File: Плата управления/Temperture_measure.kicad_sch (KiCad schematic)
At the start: 3 parts

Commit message: Версия под отчёт
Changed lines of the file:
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@@
   )
   (text "Температура транзисторов" (at 137.795 76.2 0)
-    (effects (font (size 2 2) bold) (justify left bottom))
+    (effects (font (size 2.5 2.5) bold) (justify left bottom))
   )
   (global_label "Temperature_Power_SDA_MCU" (shape bidirectional) (at 157.48 107.315 0) (fields_autoplaced)

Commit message: VER2.0
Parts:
- removed R17, R18, R19: 10k, Resistor_SMD:R_0603_1608Metric_Pad0.98x0.95mm_HandSolder, symbol Device:R_Small
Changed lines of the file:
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@@
     (comment 1 "МПСТ.76721.758764.02.Э3.М")
-  )
-  (junction (at 139.7 93.345) (diameter 0) (color 0 0 0 0)
-  )
-  (wire (pts (xy 157.48 107.315) (xy 130.81 107.315))
-    (stroke (width 0) (type default))
-  )
-  (wire (pts (xy 157.48 102.235) (xy 148.59 102.235))
-    (stroke (width 0) (type default))
-  )
-  (wire (pts (xy 139.7 93.345) (xy 139.7 94.615))
-    (stroke (width 0) (type default))
-  )
-  (wire (pts (xy 139.7 92.075) (xy 139.7 93.345))
-    (stroke (width 0) (type default))
-  )
-  (wire (pts (xy 139.7 104.775) (xy 139.7 99.695))
-    (stroke (width 0) (type default))
-  )
-  (wire (pts (xy 148.59 94.615) (xy 148.59 93.345))
-    (stroke (width 0) (type default))
-  )
-  (wire (pts (xy 148.59 102.235) (xy 148.59 99.695))
-    (stroke (width 0) (type default))
-  )
-  (wire (pts (xy 130.81 93.345) (xy 139.7 93.345))
-    (stroke (width 0) (type default))
-  )
-  (wire (pts (xy 139.7 93.345) (xy 148.59 93.345))
-    (stroke (width 0) (type default))
-  )
-  (wire (pts (xy 130.81 94.615) (xy 130.81 93.345))
-    (stroke (width 0) (type default))
-  )
-  (wire (pts (xy 130.81 107.315) (xy 130.81 99.695))
-    (stroke (width 0) (type default))
-  )
-  (wire (pts (xy 157.48 104.775) (xy 139.7 104.775))
-    (stroke (width 0) (type default))
   )
   (rectangle (start 125.095 76.835) (end 190.5 121.285)
@@
     (effects (font (size 2.5 2.5) bold) (justify left bottom))
   )
-  (global_label "Temperature_Power_SDA_MCU" (shape bidirectional) (at 157.48 107.315 0) (fields_autoplaced)
-    (effects (font (size 1.27 1.27)) (justify left))
-    (property "Intersheetrefs" "${INTERSHEET_REFS}" (at 189.3954 107.315 0)
-      (effects (font (size 1.27 1.27)) (justify left) hide)
-    )
-  )
-  (global_label "Temperature_Power_SCL_MCU" (shape input) (at 157.48 104.775 0) (fields_autoplaced)
-    (effects (font (size 1.27 1.27)) (justify left))
-    (property "Intersheetrefs" "${INTERSHEET_REFS}" (at 188.2236 104.775 0)
-      (effects (font (size 1.27 1.27)) (justify left) hide)
-    )
-  )
-  (global_label "Temperature_Power_~{OS}_MCU" (shape input) (at 157.48 102.235 0) (fields_autoplaced)
-    (effects (font (size 1.27 1.27)) (justify left))
-    (property "Intersheetrefs" "${INTERSHEET_REFS}" (at 187.256 102.235 0)
-      (effects (font (size 1.27 1.27)) (justify left) hide)
-    )
-  )
-  (symbol (lib_id "Device:R_Small") (at 148.59 97.155 180) (unit 1)
-    (in_bom yes) (on_board yes) (dnp no) (fields_autoplaced)
-    (property "Reference" "R19" (at 151.13 96.52 0)
-      (effects (font (size 1.27 1.27)) (justify right))
-    )
-    (property "Value" "10k" (at 151.13 99.06 0)
-      (effects (font (size 1.27 1.27)) (justify right))
-    )
-    (property "Footprint" "Resistor_SMD:R_0603_1608Metric_Pad0.98x0.95mm_HandSolder" (at 148.59 97.155 0)
-      (effects (font (size 1.27 1.27)) hide)
-    )
-    (property "Datasheet" "~" (at 148.59 97.155 0)
-      (effects (font (size 1.27 1.27)) hide)
-    )
-    (pin "1")
-    (pin "2")
-    (instances
-      (project "Плата управления"
-        (path "/75f4c67c-bbde-4446-8f82-67797a1b269f/d6b8b9ce-300b-4d22-9d4c-9182eba581b1"
-          (reference "R19") (unit 1)
-        )
-        (path "/75f4c67c-bbde-4446-8f82-67797a1b269f/c91ff3ec-ad20-4326-acd4-2c9dea437172"
-          (reference "R17") (unit 1)
-        )
-      )
-      (project "Силовая плата"
-        (path "/96c6fc92-8ec6-44f7-b0dc-9ad8f1acea09/1efb5faf-bb82-4ac6-a144-d6576b4720aa"
-          (reference "R2") (unit 1)
-        )
-      )
-    )
-  )
-  (symbol (lib_id "power:+3.3V") (at 139.7 92.075 0) (unit 1)
-    (in_bom yes) (on_board yes) (dnp no) (fields_autoplaced)
-    (property "Reference" "#PWR026" (at 139.7 95.885 0)
-      (effects (font (size 1.27 1.27)) hide)
-    )
-    (property "Value" "+3.3V" (at 139.7 88.265 0)
-      (effects (font (size 1.27 1.27)))
-    )
-    (property "Footprint" "" (at 139.7 92.075 0)
-      (effects (font (size 1.27 1.27)) hide)
-    )
-    (property "Datasheet" "" (at 139.7 92.075 0)
-      (effects (font (size 1.27 1.27)) hide)
-    )
-    (pin "1")
-    (instances
-      (project "Плата управления"
-        (path "/75f4c67c-bbde-4446-8f82-67797a1b269f/d6b8b9ce-300b-4d22-9d4c-9182eba581b1"
-          (reference "#PWR026") (unit 1)
-        )
-      )
-    )
-  )
-  (symbol (lib_id "Device:R_Small") (at 130.81 97.155 180) (unit 1)
-    (in_bom yes) (on_board yes) (dnp no) (fields_autoplaced)
-    (property "Reference" "R17" (at 133.35 96.52 0)
-      (effects (font (size 1.27 1.27)) (justify right))
-    )
-    (property "Value" "10k" (at 133.35 99.06 0)
-      (effects (font (size 1.27 1.27)) (justify right))
-    )
-    (property "Footprint" "Resistor_SMD:R_0603_1608Metric_Pad0.98x0.95mm_HandSolder" (at 130.81 97.155 0)
-      (effects (font (size 1.27 1.27)) hide)
-    )
-    (property "Datasheet" "~" (at 130.81 97.155 0)
-      (effects (font (size 1.27 1.27)) hide)
-    )
-    (pin "1")
-    (pin "2")
-    (instances
-      (project "Плата управления"
-        (path "/75f4c67c-bbde-4446-8f82-67797a1b269f/d6b8b9ce-300b-4d22-9d4c-9182eba581b1"
-          (reference "R17") (unit 1)
-        )
-        (path "/75f4c67c-bbde-4446-8f82-67797a1b269f/c91ff3ec-ad20-4326-acd4-2c9dea437172"
-          (reference "R17") (unit 1)
-        )
-      )
-      (project "Силовая плата"
-        (path "/96c6fc92-8ec6-44f7-b0dc-9ad8f1acea09/1efb5faf-bb82-4ac6-a144-d6576b4720aa"
-          (reference "R2") (unit 1)
-        )
-      )
-    )
-  )
-  (symbol (lib_id "Device:R_Small") (at 139.7 97.155 180) (unit 1)
-    (in_bom yes) (on_board yes) (dnp no) (fields_autoplaced)
-    (property "Reference" "R18" (at 142.24 96.52 0)
-      (effects (font (size 1.27 1.27)) (justify right))
-    )
-    (property "Value" "10k" (at 142.24 99.06 0)
-      (effects (font (size 1.27 1.27)) (justify right))
-    )
-    (property "Footprint" "Resistor_SMD:R_0603_1608Metric_Pad0.98x0.95mm_HandSolder" (at 139.7 97.155 0)
-      (effects (font (size 1.27 1.27)) hide)
-    )
-    (property "Datasheet" "~" (at 139.7 97.155 0)
-      (effects (font (size 1.27 1.27)) hide)
-    )
-    (pin "1")
-    (pin "2")
-    (instances
-      (project "Плата управления"
-        (path "/75f4c67c-bbde-4446-8f82-67797a1b269f/d6b8b9ce-300b-4d22-9d4c-9182eba581b1"
-          (reference "R18") (unit 1)
-        )
-        (path "/75f4c67c-bbde-4446-8f82-67797a1b269f/c91ff3ec-ad20-4326-acd4-2c9dea437172"
-          (reference "R17") (unit 1)
-        )
-      )
-      (project "Силовая плата"
-        (path "/96c6fc92-8ec6-44f7-b0dc-9ad8f1acea09/1efb5faf-bb82-4ac6-a144-d6576b4720aa"
-          (reference "R2") (unit 1)
-        )
-      )
-    )
-  )
 )

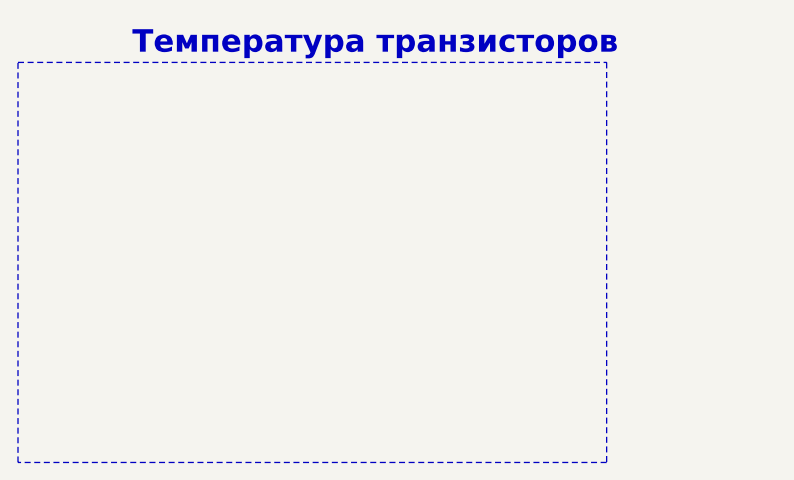
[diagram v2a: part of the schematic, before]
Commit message: Добавил NTC обработку
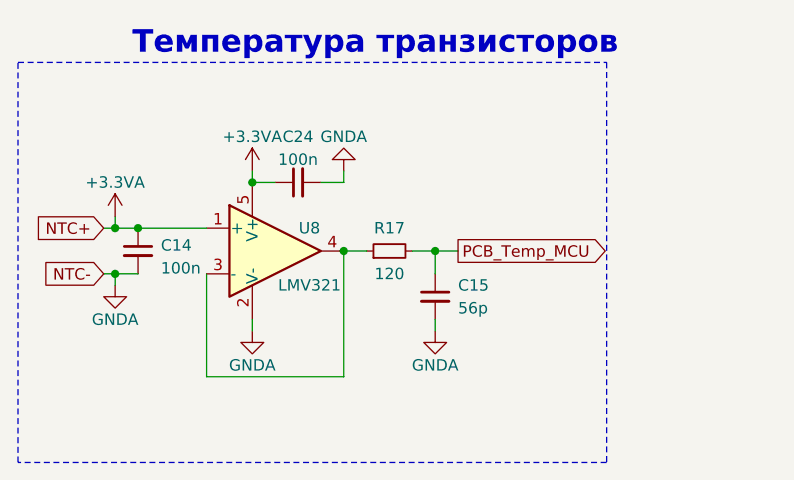
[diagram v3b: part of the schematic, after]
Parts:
- added C14, C24: 100n, Capacitor_SMD:C_0603_1608Metric_Pad1.08x0.95mm_HandSolder, symbol Device:C_Small
- added C15: 56p, Capacitor_SMD:C_0603_1608Metric_Pad1.08x0.95mm_HandSolder, symbol Device:C_Small
- added R17: 120, Resistor_SMD:R_0603_1608Metric_Pad0.98x0.95mm_HandSolder, symbol Device:R_Small
- added U8: LMV321, Package_TO_SOT_SMD:SOT-23-5_HandSoldering, symbol Amplifier_Operational:LMV321
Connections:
- new net: R17.1, U8.3 (-), U8.4
- new net +3.3VA: C14.1, C24.1, U8.1 (+), U8.5 (V+)
- new net GNDA: C14.2, C15.2, C24.2, U8.2 (V-)
- new net PCB_Temp_MCU: C15.1, R17.2

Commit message: Новые драйвера и разъёмы
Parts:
- added C42, C43, C47, C50: 100n, Capacitor_SMD:C_0603_1608Metric_Pad1.08x0.95mm_HandSolder, symbol Device:C_Small
- added C45, C51: 56p, Capacitor_SMD:C_0603_1608Metric_Pad1.08x0.95mm_HandSolder, symbol Device:C_Small
- added R18, R19: 120, Resistor_SMD:R_0603_1608Metric_Pad0.98x0.95mm_HandSolder, symbol Device:R_Small
- added R23, R24, R25: 10k, Resistor_SMD:R_0603_1608Metric_Pad0.98x0.95mm_HandSolder, symbol Device:R_Small
- added U1, U2: LMV321, Package_TO_SOT_SMD:SOT-23-5_HandSoldering, symbol Amplifier_Operational:LMV321
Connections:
- net +3.3VA: now also C43.1, C50.1, U1.5 (V+), U2.5 (V+); no longer C14.1, U8.1 (+)
- net GNDA: now also C14.1, C42.1, C43.2, C45.2, C47.1, C50.2, C51.2, R23.1, R24.1, R25.1, U1.2 (V-), U2.2 (V-); no longer C14.2
- net PCB_Temp_MCU renamed PCB_Temp_A_MCU
- new net: R19.1, U2.3 (-), U2.4
- new net: R18.1, U1.3 (-), U1.4
- new net NTC_A-: C14.2, R23.2, U8.1 (+)
- new net NTC_B-: C42.2, R24.2, U1.1 (+)
- new net NTC_C-: C47.2, R25.2, U2.1 (+)
- new net PCB_Temp_B_MCU: C45.1, R18.2
- new net PCB_Temp_C_MCU: C51.1, R19.2
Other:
- note added: "Температура силовой платы A"
- note added: "Температура силовой платы B"
- note added: "Температура силовой платы C"
- note removed: "Температура транзисторов"
- moved on the sheet: C14, C15, C24, R17, U8
